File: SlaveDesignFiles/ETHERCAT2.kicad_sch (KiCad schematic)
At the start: 33 parts

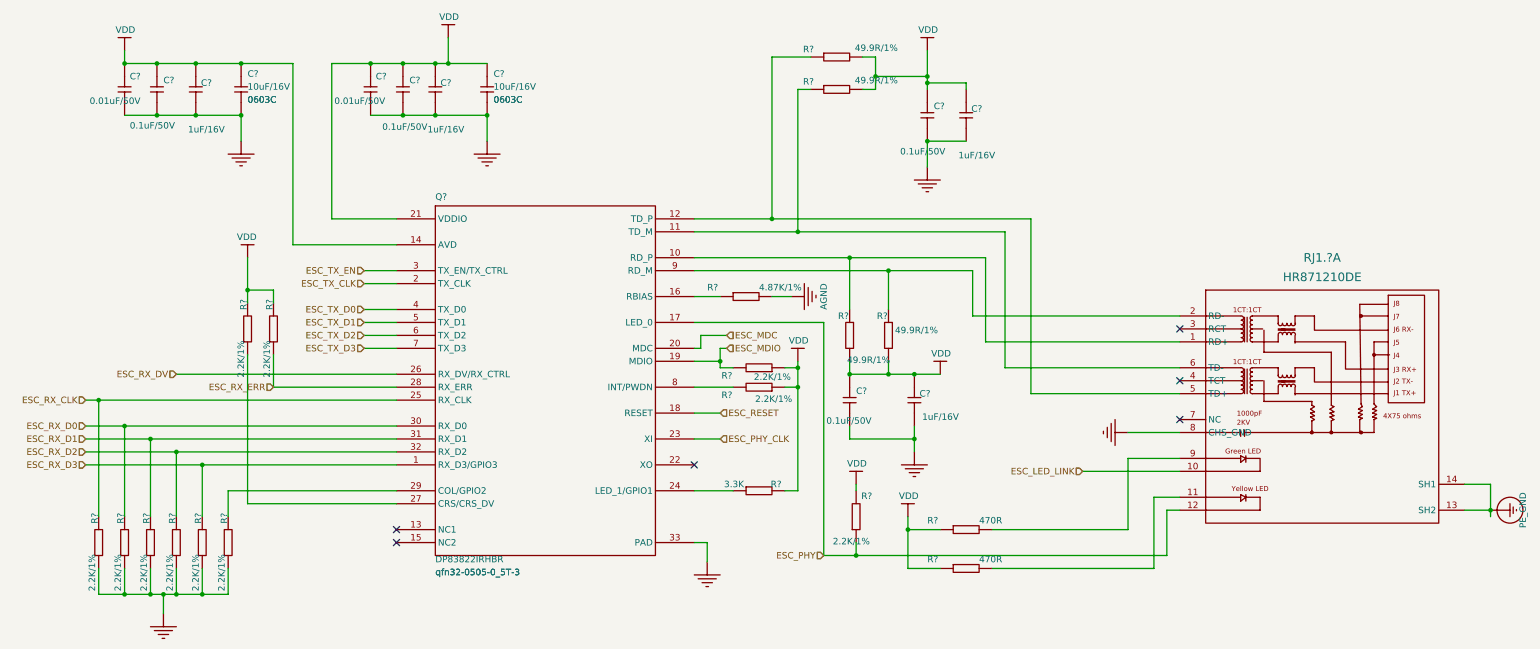
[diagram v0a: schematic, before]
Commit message: 1. 在USB处，修改了type-c5V输入的定义，添加了二极管；2. 将CJA1117B-3.3替换为AMS1117-3.3；3. 分配了testpoint的封装；4. 修改了H485，can插件的PE_GNG引脚定义。
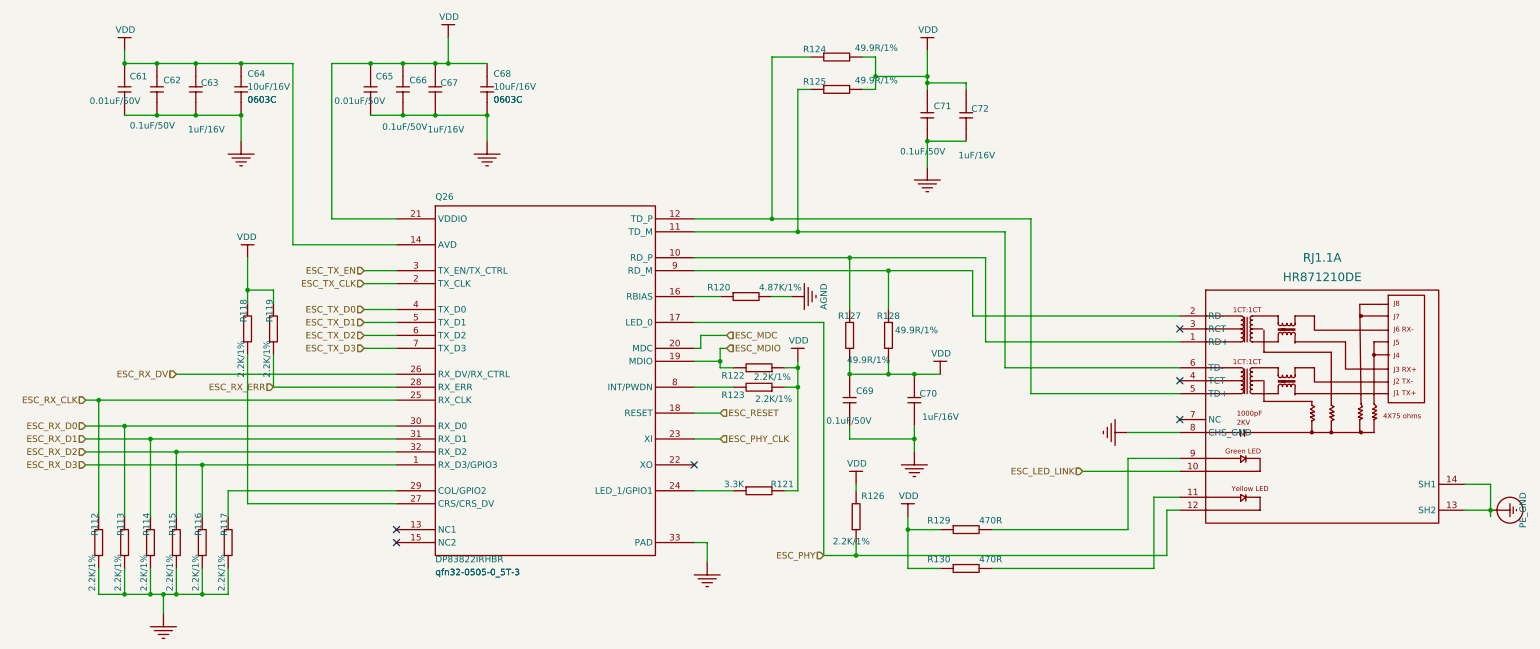
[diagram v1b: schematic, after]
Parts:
- gave numbers to parts that had none: 33

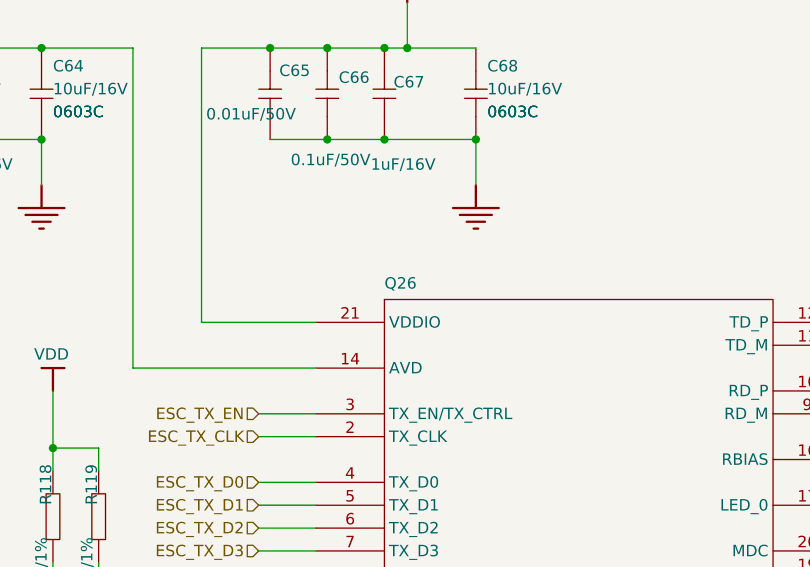
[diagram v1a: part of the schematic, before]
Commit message: Fix bugs in PWM subsheet
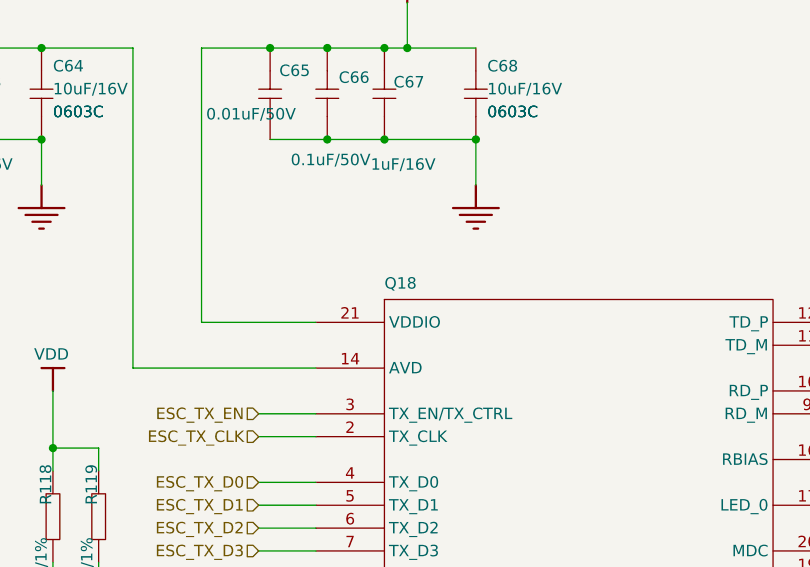
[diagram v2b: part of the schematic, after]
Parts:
- renumbered Q26 to Q18
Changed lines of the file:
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@@
 		(on_board yes)
 		(dnp no)
-		(property "Reference" "Q26"
+		(property "Reference" "Q18"
 			(at 93.98 50.8 0)
 			(effects
@@
 			(project "sheet1"
 				(path "/54840d93-b842-4275-b1cb-4ec5510cbfff/49c4ce84-2d31-456a-8e91-ba3517e8f87a"
-					(reference "Q26")
+					(reference "Q18")
 					(unit 1)
 				)
